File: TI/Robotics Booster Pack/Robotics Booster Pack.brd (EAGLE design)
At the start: 68.6 x 76.2 mm, 119 parts, among them U10 74LVTH125.RGY, U11 SCHA4B0400, U12 BLUETOOTH-RN41", U13 XBEE-1XBEE-1_LOCK, U5 TPS5331[8/9].DQP, U6 TPS62082.DSG, U7 PCA9557.RGV, U8 MPU-6050

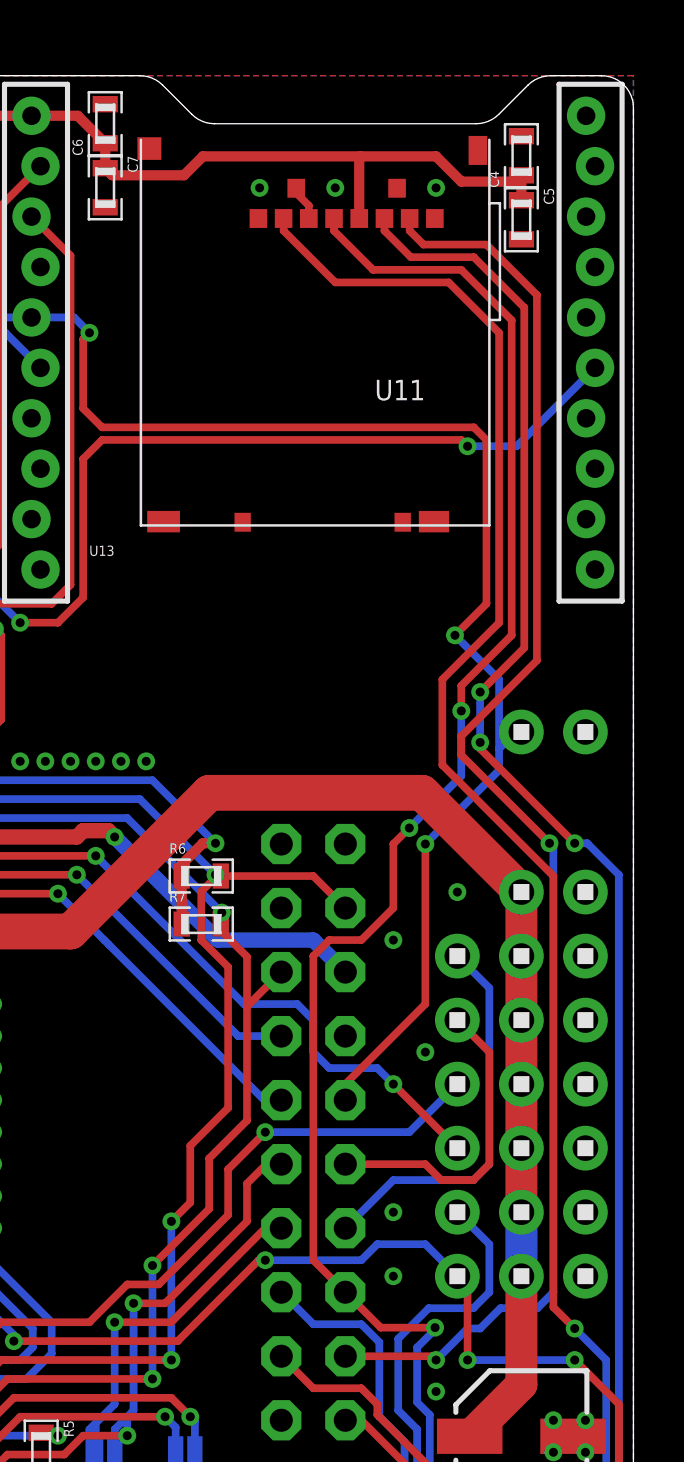
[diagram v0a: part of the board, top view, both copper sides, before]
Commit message: Renamed files. Corrected uSD Card package. All other ICs check out.
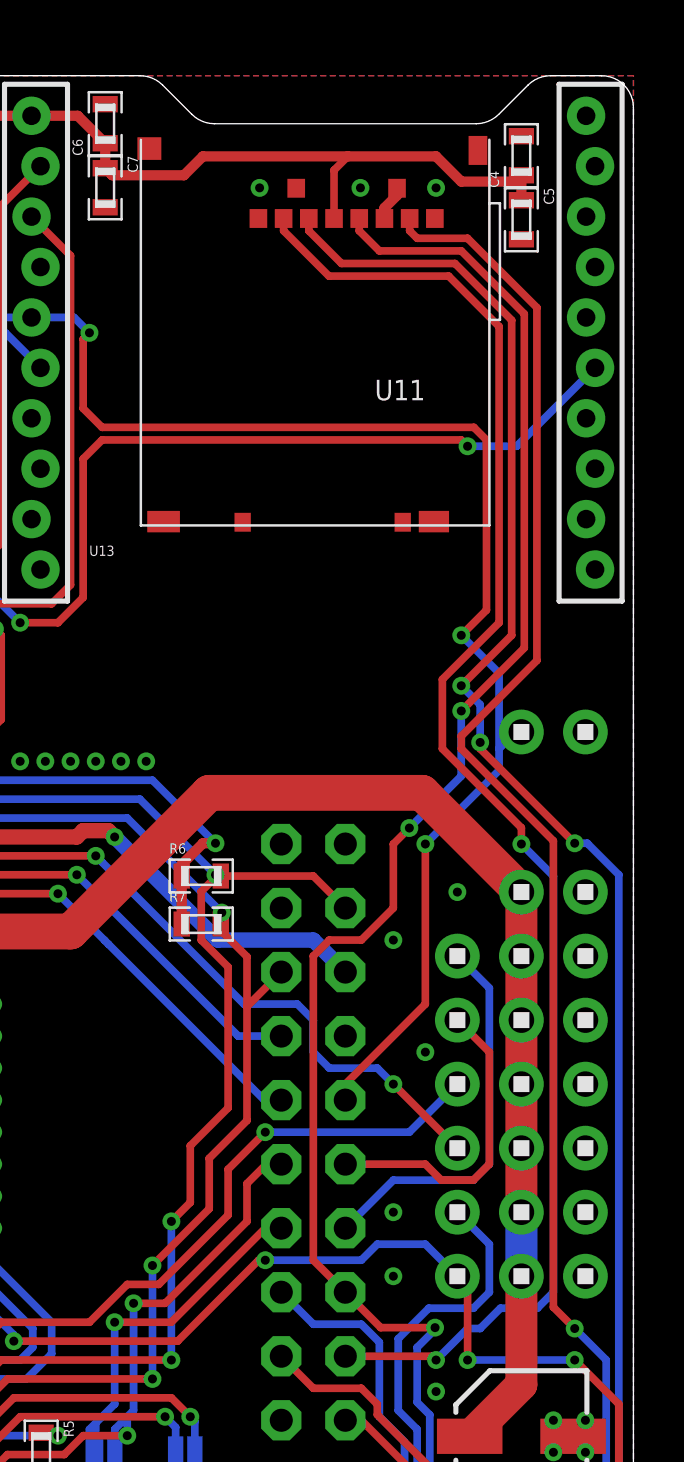
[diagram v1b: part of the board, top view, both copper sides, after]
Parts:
- C32: value 10nF -> 2.2uF
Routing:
- net SPI.MISO: track 159.0 -> 156.1 mm
- net SPI.FSS: track 58.3 -> 61.1 mm
- net SPI.MOSI: track 165.0 -> 167.7 mm

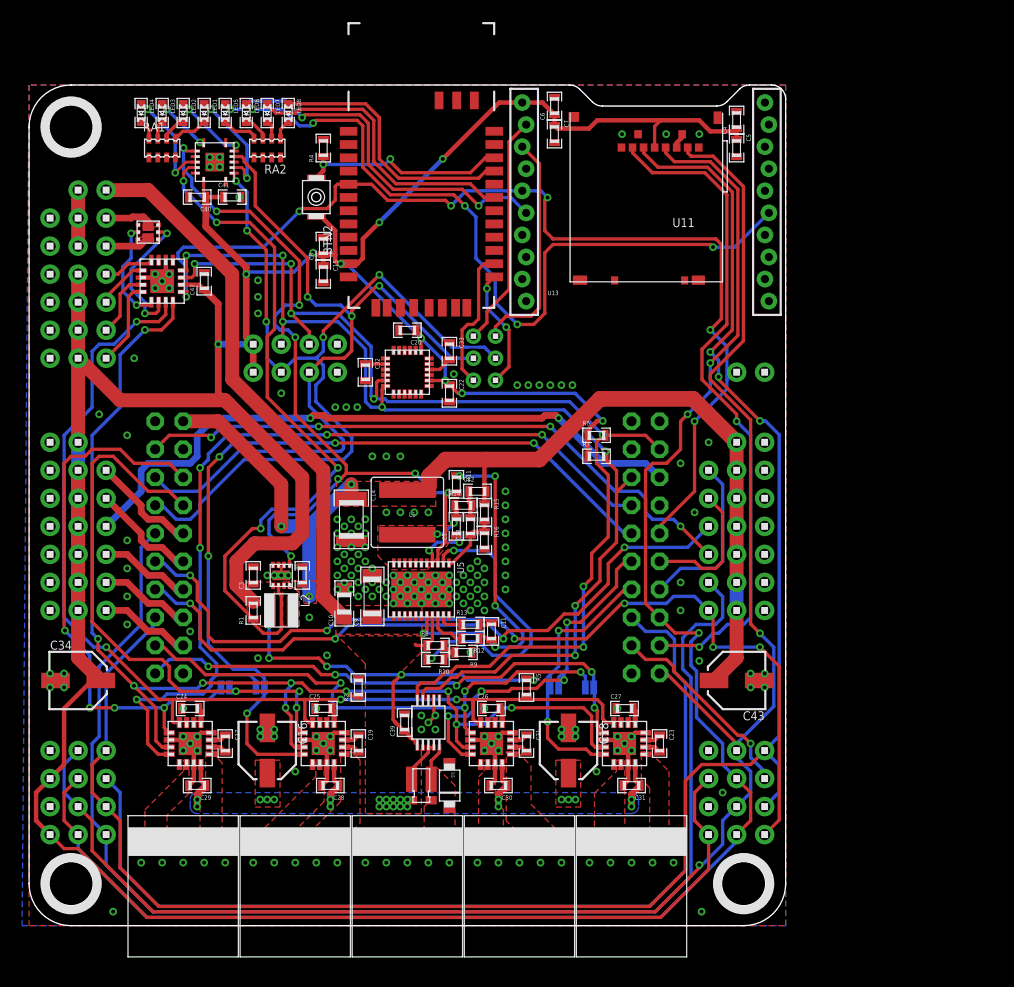
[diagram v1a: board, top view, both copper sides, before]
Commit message: Creating base board for Pololu Black Motor Mount
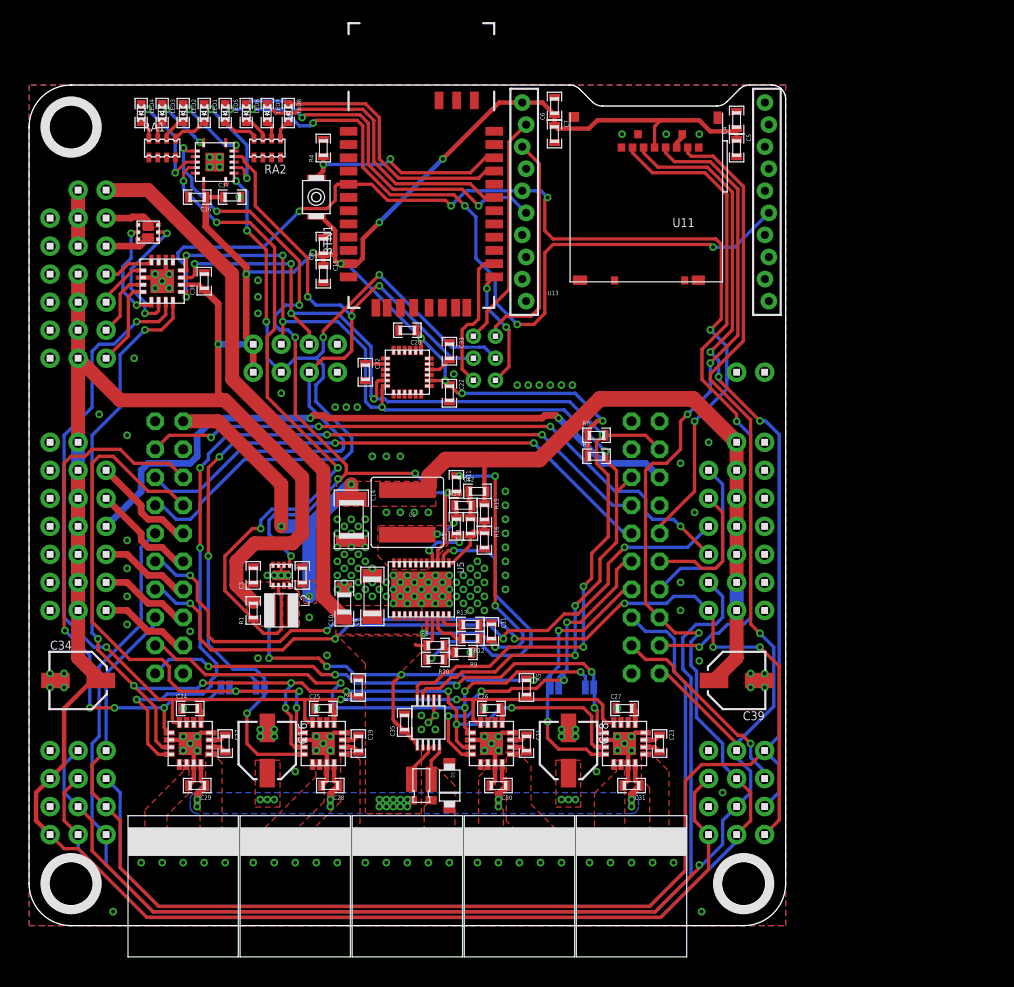
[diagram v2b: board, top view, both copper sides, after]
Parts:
- removed C43: 100uF, microbuilder:PANASONIC_C
- added C35: .1uF, standardparts:0603
- C39: value .1uF -> 100uF; device standardparts:0603 -> microbuilder:PANASONIC_C
- U1, U2, U3, U4: value (none) -> DRV8800
- moved C39 30.3 mm to (64.1, 22.2), turned to 180 degrees
- renumbered BTN2 to BTN1, C40 to C36, C41 to C37, C42 to C38, U$118 to U9, U$55 to U14
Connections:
- net 3.3V: now also C35.1; no longer C39.1
- net 5.0V: now also C39.+; no longer C43.+
- net GND: now also C35.2, C39.-; no longer C39.2, C43.-
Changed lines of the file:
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@@
 <element name="U$11" library="screw_holes" package="4MM" value="HOLE.4MM" x="3.81" y="72.39"/>
 <element name="U13" library="SparkFun-RF" package="XBEE-1_LOCK" value="XBEE-1XBEE-1_LOCK" x="55.88" y="54.61"/>
-<element name="U1" library="packages(ti)" package="RTY.16" value="" x="14.605" y="16.51"/>
-<element name="U2" library="packages(ti)" package="RTY.16" value="" x="26.67" y="16.51"/>
-<element name="U3" library="packages(ti)" package="RTY.16" value="" x="41.91" y="16.51"/>
-<element name="U4" library="packages(ti)" package="RTY.16" value="" x="53.975" y="16.51"/>
+<element name="U1" library="packages(ti)" package="RTY.16" value="DRV8800" x="14.605" y="16.51"/>
+<element name="U2" library="packages(ti)" package="RTY.16" value="DRV8800" x="26.67" y="16.51"/>
+<element name="U3" library="packages(ti)" package="RTY.16" value="DRV8800" x="41.91" y="16.51"/>
+<element name="U4" library="packages(ti)" package="RTY.16" value="DRV8800" x="53.975" y="16.51"/>
 <element name="U11" library="alps" package="SCHA4B0400" value="SCHA4B0400" x="62.865" y="73.66" rot="R180"/>
 <element name="H1" library="headers(.1in)" package="1X6" value="1X6" x="66.675" y="28.575" rot="R90"/>
@@
 <element name="H14" library="headers(.1in)" package="2X3" value="2X3" x="61.595" y="13.335"/>
 <element name="H16" library="headers(.1in)" package="2X3" value="2X3" x="61.595" y="8.255"/>
-<element name="U$55" library="freescale" package="MICROFET.2X2" value="FDMA1024NZ" x="10.795" y="62.865" rot="R270"/>
+<element name="U14" library="freescale" package="MICROFET.2X2" value="FDMA1024NZ" x="10.795" y="62.865" rot="R270"/>
 <element name="U8" library="invensense" package="QFN.24.4X4" value="MPU-6050" x="34.29" y="50.165" rot="R90"/>
 <element name="H21" library="phoenixcontact" package="PTS.PLUG" value="1X2.PTS" x="34.29" y="7.62" rot="R180"/>
@@
 <element name="C33" library="standardparts" package="0603" value=".1uF" x="38.1" y="52.07" rot="R270"/>
 <element name="R3" library="vishay" package="0612" value="1u" x="35.56" y="12.7" rot="R270"/>
-<element name="U$118" library="packages(ti)" package="DGS.10" value="INA220.DGS" x="36.195" y="18.415" rot="R180"/>
-<element name="C39" library="standardparts" package="0603" value=".1uF" x="34.036" y="18.415" rot="R90"/>
+<element name="U9" library="packages(ti)" package="DGS.10" value="INA220.DGS" x="36.195" y="18.415" rot="R180"/>
+<element name="C35" library="standardparts" package="0603" value=".1uF" x="34.036" y="18.415" rot="R90"/>
 <element name="U7" library="packages(ti)" package="RGV.16" value="PCA9557.RGV" x="12.065" y="58.42" rot="R270"/>
-<element name="C42" library="standardparts" package="0603" value=".1uF" x="15.875" y="58.42" rot="R90"/>
+<element name="C38" library="standardparts" package="0603" value=".1uF" x="15.875" y="58.42" rot="R90"/>
 <element name="LED1" library="standardparts" package="0603.LED" value="" x="15.875" y="73.66" rot="R270"/>
 <element name="LED2" library="standardparts" package="0603.LED" value="" x="13.97" y="73.66" rot="R270"/>
@@
 <element name="RA2" library="resistorarray" package="0603.4.C" value="1k" x="21.59" y="70.485" rot="R180"/>
 <element name="R4" library="standardparts" package="0603" value="1k" x="26.67" y="70.485" rot="R90"/>
-<element name="BTN2" library="omron" package="B3U-1000P(M)-B" value="B3U-1000P(M)-B" x="26.035" y="66.04" rot="R270"/>
+<element name="BTN1" library="omron" package="B3U-1000P(M)-B" value="B3U-1000P(M)-B" x="26.035" y="66.04" rot="R270"/>
 <element name="H24" library="headers(.1in)" package="1X2" value="1X2" x="64.135" y="50.165"/>
 <element name="R5" library="standardparts" package="0603" value="100k" x="45.085" y="21.59" rot="R270"/>
-<element name="C40" library="standardparts" package="0603" value=".1uF" x="15.24" y="66.04" rot="R180"/>
-<element name="C41" library="standardparts" package="0603" value="1uF" x="18.415" y="66.04"/>
+<element name="C36" library="standardparts" package="0603" value=".1uF" x="15.24" y="66.04" rot="R180"/>
+<element name="C37" library="standardparts" package="0603" value="1uF" x="18.415" y="66.04"/>
 <element name="R6" library="standardparts" package="0603" value="2.2k" x="51.435" y="44.45"/>
 <element name="R7" library="standardparts" package="0603" value="2.2k" x="51.435" y="42.545"/>
-<element name="C43" library="microbuilder" package="PANASONIC_C" value="100uF" x="64.135" y="22.225" rot="R180"/>
+<element name="C39" library="microbuilder" package="PANASONIC_C" value="100uF" x="64.135" y="22.225" rot="R180"/>
 <element name="U$6" library="headers(.1in)" package="1X4" value="1X4" x="20.32" y="52.705"/>
 <element name="U$7" library="headers(.1in)" package="1X4" value="1X4" x="20.32" y="50.165"/>
@@
 <contactref element="C20" pad="1"/>
 <contactref element="U8" pad="8"/>
-<contactref element="U$118" pad="6"/>
-<contactref element="C39" pad="1"/>
+<contactref element="U9" pad="6"/>
+<contactref element="C35" pad="1"/>
 <contactref element="U7" pad="14"/>
-<contactref element="C42" pad="1"/>
+<contactref element="C38" pad="1"/>
 <contactref element="U10" pad="14"/>
-<contactref element="BTN2" pad="2"/>
-<contactref element="C40" pad="1"/>
-<contactref element="C41" pad="1"/>
+<contactref element="BTN1" pad="2"/>
+<contactref element="C36" pad="1"/>
+<contactref element="C37" pad="1"/>
 <contactref element="R6" pad="1"/>
 <contactref element="R7" pad="1"/>
@@
 <contactref element="U13" pad="10"/>
 <polygon width="0.254" layer="16" rank="6">
-<vertex x="-0.635" y="0"/>
+<vertex x="0" y="0"/>
 <vertex x="68.58" y="0"/>
 <vertex x="68.58" y="76.2"/>
@@
 <contactref element="H16" pad="2"/>
 <contactref element="H14" pad="2"/>
-<contactref element="U$55" pad="4"/>
-<contactref element="U$55" pad="1"/>
+<contactref element="U14" pad="4"/>
+<contactref element="U14" pad="1"/>
 <contactref element="U2" pad="2"/>
 <contactref element="U2" pad="PAD"/>
@@
 <contactref element="C20" pad="2"/>
 <contactref element="C22" pad="2"/>
-<contactref element="U$118" pad="7"/>
-<contactref element="U$118" pad="2"/>
-<contactref element="U$118" pad="1"/>
-<contactref element="C39" pad="2"/>
+<contactref element="U9" pad="7"/>
+<contactref element="U9" pad="2"/>
+<contactref element="U9" pad="1"/>
+<contactref element="C35" pad="2"/>
 <contactref element="H1" pad="1"/>
 <contactref element="H1" pad="6"/>
@@
 <contactref element="U7" pad="1"/>
 <contactref element="U7" pad="2"/>
-<contactref element="C42" pad="2"/>
+<contactref element="C38" pad="2"/>
 <contactref element="U10" pad="PAD"/>
 <contactref element="U10" pad="7"/>
@@
 <contactref element="H10" pad="3"/>
 <contactref element="H10" pad="2"/>
-<contactref element="C40" pad="2"/>
-<contactref element="C41" pad="2"/>
+<contactref element="C36" pad="2"/>
+<contactref element="C37" pad="2"/>
 <contactref element="RA2" pad="2"/>
 <contactref element="RA2" pad="4"/>
 <contactref element="RA2" pad="6"/>
 <contactref element="RA2" pad="8"/>
-<contactref element="C43" pad="-"/>
+<contactref element="C39" pad="-"/>
 <contactref element="U$7" pad="4"/>
 <contactref element="U$6" pad="4"/>
@@
 </signal>
 <signal name="FET0.G">
-<contactref element="U$55" pad="2"/>
+<contactref element="U14" pad="2"/>
 <contactref element="U7" pad="9"/>
 <via x="9.75" y="56.25" extent="1-16" drill="0.3556"/>
@@
 </signal>
 <signal name="FET1.G">
-<contactref element="U$55" pad="5"/>
+<contactref element="U14" pad="5"/>
 <contactref element="U7" pad="10"/>
 <wire x1="11.74" y1="56.52" x2="11.74" y2="55.74" width="0.3048" layer="1"/>
@@
 <vertex x="27.865" y="38.02"/>
 </polygon>
-<contactref element="C43" pad="+"/>
+<contactref element="C39" pad="+"/>
 <wire x1="64.135" y1="43.815" x2="64.135" y2="41.275" width="1.27" layer="1"/>
 <wire x1="64.135" y1="41.275" x2="64.135" y2="38.735" width="1.27" layer="1"/>
@@
 <contactref element="U12" pad="22"/>
 <contactref element="R4" pad="1"/>
-<contactref element="BTN2" pad="1"/>
+<contactref element="BTN1" pad="1"/>
 <wire x1="26.67" y1="69.71" x2="26.67" y2="69" width="0.4064" layer="1"/>
 <wire x1="26.67" y1="69" x2="26.67" y2="68.425" width="0.4064" layer="1"/>
@@
 <contactref element="R3" pad="2@1"/>
 <contactref element="R3" pad="2@2"/>
-<contactref element="U$118" pad="9"/>
-<contactref element="U$118" pad="8"/>
+<contactref element="U9" pad="9"/>
+<contactref element="U9" pad="8"/>
 <polygon width="0.254" layer="1" thermals="no">
 <vertex x="27.813" y="29.02"/>
@@
 <contactref element="U8" pad="24"/>
 <contactref element="U7" pad="16"/>
-<contactref element="U$118" pad="4"/>
+<contactref element="U9" pad="4"/>
 <contactref element="R7" pad="2"/>
 <contactref element="U$6" pad="2"/>
@@
 <contactref element="U8" pad="23"/>
 <contactref element="U7" pad="15"/>
-<contactref element="U$118" pad="5"/>
+<contactref element="U9" pad="5"/>
 <contactref element="R6" pad="2"/>
 <contactref element="U$6" pad="3"/>
@@
 <contactref element="R3" pad="1@2"/>
 <contactref element="R3" pad="1@1"/>
-<contactref element="U$118" pad="10"/>
+<contactref element="U9" pad="10"/>
 <polygon width="0.254" layer="1" thermals="no">
 <vertex x="35.814" y="6.604"/>
@@
 </signal>
 <signal name="FET0.D">
-<contactref element="U$55" pad="6"/>
-<contactref element="U$55" pad="PAD@1"/>
+<contactref element="U14" pad="6"/>
+<contactref element="U14" pad="PAD@1"/>
 <contactref element="H9" pad="1"/>
 <polygon width="0.254" layer="1" thermals="no">
@@
 </signal>
 <signal name="FET1.D">
-<contactref element="U$55" pad="PAD@2"/>
-<contactref element="U$55" pad="3"/>
+<contactref element="U14" pad="PAD@2"/>
+<contactref element="U14" pad="3"/>
 <contactref element="H9" pad="2"/>
 <polygon width="0.254" layer="1" thermals="no">
